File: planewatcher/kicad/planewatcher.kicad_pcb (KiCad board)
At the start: 4 copper layers, 86.1 x 54 mm, 154 parts, among them J1 1PPS_OUT, J2 RF_IN, J3 BMI-S-209-F + C, J4 FPGA BANK 33, J5 FPGA BANK 35 V1.2/V1.3, J6 GPS _IN, U1 LEA-M8T, U10 AD8138, U11 AD9203, U2 AP22653AW6-7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

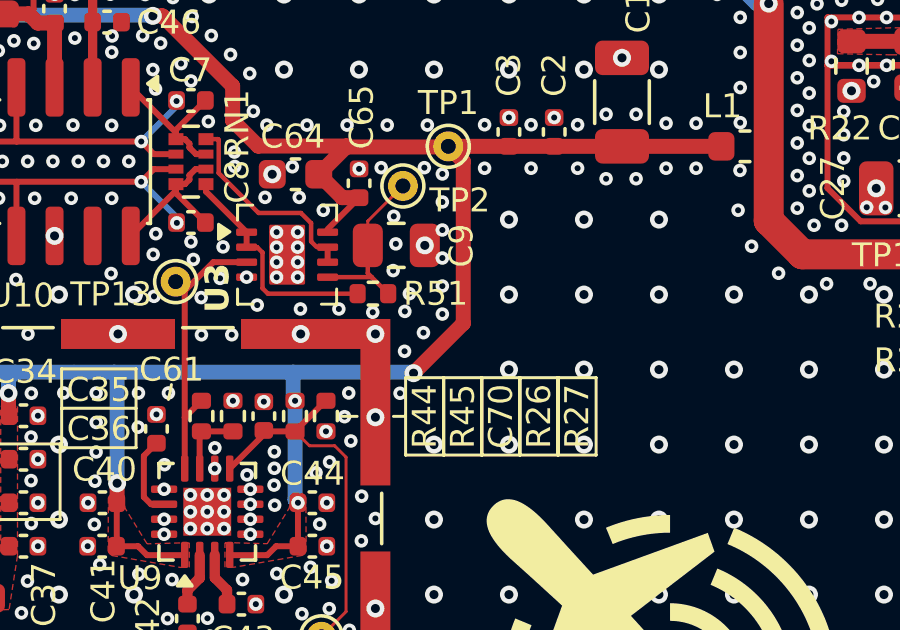
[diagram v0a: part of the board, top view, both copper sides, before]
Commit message: Slow down the LPF to avoid artificially raising the noise-floor baseline in high traffic areas
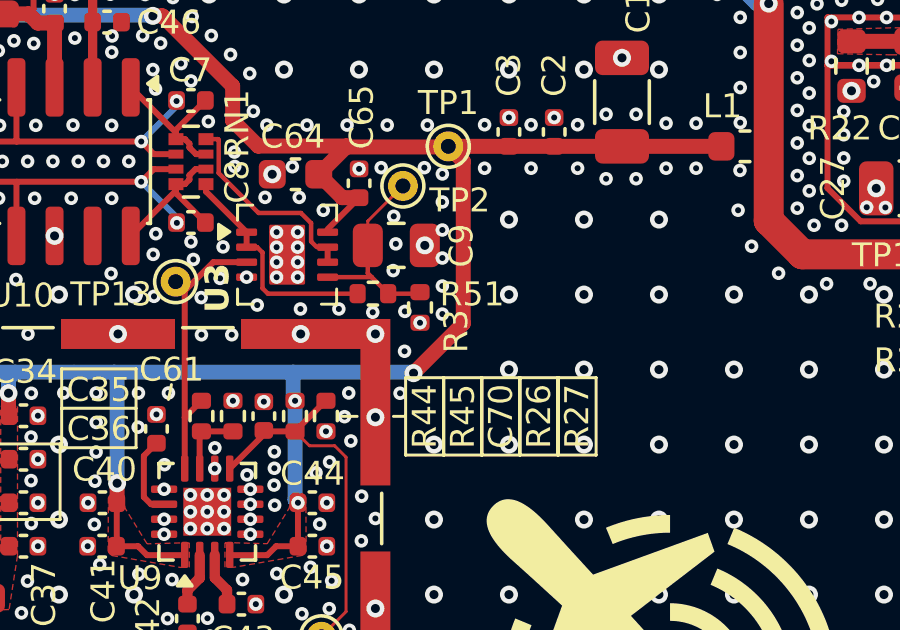
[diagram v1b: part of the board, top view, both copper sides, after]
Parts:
- added R3: R_BASE_GND_DNP, Resistor_SMD:R_0402_1005Metric, F.Cu at (144.5, 90.4)
- C9: value 1µF -> 2.2µF
- R51: value 100kΩ -> 1MΩ
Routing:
- net Net-(U3B-+INB): track 5.83 -> 6.91 mm
- net GND: vias 1851 -> 1850
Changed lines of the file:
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@@
 		)
 	)
+	(footprint "Resistor_SMD:R_0402_1005Metric"
+		(layer "F.Cu")
+		(at 144.535 90.43 -90)
+		(descr "Resistor SMD 0402 (1005 Metric), square (rectangular) end terminal, IPC-7351 nominal, (Body size source: IPC-SM-782 page 72, https://www.pcb-3d.com/wordpress/wp-content/uploads/ipc-sm-782a_amendment_1_and_2.pdf)")
+		(tags "resistor")
+		(property "Reference" "R3"
+			(at 0.79 -1.205 90)
+			(layer "F.SilkS")
+			(effects
+				(font
+					(size 0.8 0.8)
+					(thickness 0.15)
+				)
+			)
+		)
+		(property "Value" "R_BASE_GND_DNP"
+			(at 0 1.17 90)
+			(layer "F.Fab")
+			(effects
+				(font
+					(size 1 1)
+					(thickness 0.15)
+				)
+			)
+		)
+		(property "Datasheet" ""
+			(at 0 0 90)
+			(layer "F.Fab")
+			(hide yes)
+			(effects
+				(font
+					(size 1.27 1.27)
+				)
+			)
+		)
+		(property "Description" "Populating it forces the analog baseline to ground and disables moving-baseline subtraction. Leave DNP for normal operation."
+			(at 0 0 90)
+			(layer "F.Fab")
+			(hide yes)
+			(effects
+				(font
+					(size 1.27 1.27)
+				)
+			)
+		)
+		(property ki_fp_filters "R_*")
+		(sheetname "/ADC_Driver/")
+		(sheetfile "ADC_Driver.kicad_sch")
+		(units
+			(unit
+				(name "A")
+				(pins "1" "2")
+			)
+		)
+		(attr smd exclude_from_pos_files exclude_from_bom dnp)
+		(duplicate_pad_numbers_are_jumpers no)
+		(fp_line
+			(start -0.153641 0.38)
+			(end 0.153641 0.38)
+			(stroke
+				(width 0.12)
+				(type solid)
+			)
+			(layer "F.SilkS")
+		)
+		(fp_line
+			(start -0.153641 -0.38)
+			(end 0.153641 -0.38)
+			(stroke
+				(width 0.12)
+				(type solid)
+			)
+			(layer "F.SilkS")
+		)
+		(fp_rect
+			(start -0.93 -0.47)
+			(end 0.93 0.47)
+			(stroke
+				(width 0.05)
+				(type solid)
+			)
+			(fill no)
+			(layer "F.CrtYd")
+		)
+		(fp_rect
+			(start -0.525 -0.27)
+			(end 0.525 0.27)
+			(stroke
+				(width 0.1)
+				(type solid)
+			)
+			(fill no)
+			(layer "F.Fab")
+		)
+		(fp_text user "${REFERENCE}"
+			(at 0 0 90)
+			(layer "F.Fab")
+			(effects
+				(font
+					(size 0.26 0.26)
+					(thickness 0.04)
+				)
+			)
+		)
+		(pad "1" smd roundrect
+			(at -0.51 0 270)
+			(size 0.54 0.64)
+			(layers "F.Cu" "F.Mask" "F.Paste")
+			(roundrect_rratio 0.25)
+			(net "Net-(U3B-+INB)")
+			(pintype "passive")
+		)
+		(pad "2" smd roundrect
+			(at 0.51 0 270)
+			(size 0.54 0.64)
+			(layers "F.Cu" "F.Mask" "F.Paste")
+			(roundrect_rratio 0.25)
+			(net "GND")
+			(pintype "passive")
+		)
+		(embedded_fonts no)
+		(model "${KICAD10_3DMODEL_DIR}/Resistor_SMD.3dshapes/R_0402_1005Metric.step"
+			(offset
+				(xyz 0 0 0)
+			)
+			(scale
+				(xyz 1 1 1)
+			)
+			(rotate
+				(xyz 0 0 0)
+			)
+		)
+	)
 	(footprint "Capacitor_SMD:C_0402_1005Metric"
 		(layer "F.Cu")
@@
 			)
 		)
-		(property "Value" "1µF"
+		(property "Value" "2.2µF"
 			(at 0 1.68 0)
 			(layer "F.Fab")
@@
 			)
 		)
-		(property "Datasheet" ""
+		(property "Datasheet" "https://www.lcsc.com/datasheet/C5362585.pdf"
 			(at 0 0 0)
 			(layer "F.Fab")
@@
 			)
 		)
-		(property "Description" "CAP CER 1uF 50V X7R 0805"
+		(property "Description" "CAP CER 2.2uF 50V X7R 0805"
 			(at 0 0 0)
 			(layer "F.Fab")
@@
 			)
 		)
-		(property "MPN" "CL21B105KBFNNNE"
+		(property "MPN" "CL21B225KBYVPNE"
 			(at 0 0 0)
 			(unlocked yes)
@@
 			)
 		)
-		(property "lcsc_id" "C28323"
+		(property "lcsc_id" "C5362585"
 			(at 0 0 0)
 			(unlocked yes)
@@
 		(tags "resistor")
 		(property "Reference" "R51"
-			(at -2.09 0 0)
+			(at -3.305 -0.02 0)
 			(layer "F.SilkS")
 			(effects
@@
 			)
 		)
-		(property "Value" "100kΩ"
+		(property "Value" "1MΩ"
 			(at 0 1.17 0)
 			(layer "F.Fab")
@@
 			)
 		)
-		(property "Datasheet" "https://www.lcsc.com/datasheet/C481918.pdf"
+		(property "Datasheet" "https://www.lcsc.com/datasheet/C413126.pdf"
 			(at 0 0 0)
 			(layer "F.Fab")
@@
 			)
 		)
-		(property "Description" "RES 100kΩ ±1% 63mW 0402"
+		(property "Description" "RES 1000000Ω ±1% 0.1W 0402"
 			(at 0 0 0)
 			(layer "F.Fab")
@@
 			)
 		)
-		(property "MPN" "CRCW0402100KFKED"
+		(property "MPN" "ERJ2RKF1004X"
 			(at 0 0 180)
 			(unlocked yes)
@@
 			)
 		)
-		(property "Manufacturer" "VISHAY"
+		(property "Manufacturer" "PANASONIC"
 			(at 0 0 180)
 			(unlocked yes)
@@
 			)
 		)
-		(property "lcsc_id" "C481918"
+		(property "lcsc_id" "C413126"
 			(at 0 0 180)
 			(unlocked yes)
@@
 	)
 	(via
-		(at 144.65 91.27)
+		(at 144.535 90.939998)
 		(size 0.45)
 		(drill 0.2)
@@
 	)
 	(via
-		(at 144.18 89.97)
-		(size 0.45)
-		(drill 0.2)
-		(layers "F.Cu" "B.Cu")
-		(free yes)
-		(net "GND")
-	)
-	(via
 		(at 122.78 80.44)
 		(size 0.45)
@@
 	(segment
 		(start 143.475 89.97)
+		(end 144.485 89.97)
+		(width 0.15)
+		(layer "F.Cu")
+		(net "Net-(U3B-+INB)")
+	)
+	(segment
+		(start 143.475 89.97)
 		(end 142.925 89.42)
 		(width 0.15)
@@
 		(layer "F.Cu")
 		(net "Net-(U3B-+INB)")
+	)
+	(segment
+		(start 144.485 89.97)
+		(end 144.535 89.92)
+		(width 0.15)
+		(layer "F.Cu")
+		(net "Net-(U3B-+INB)")

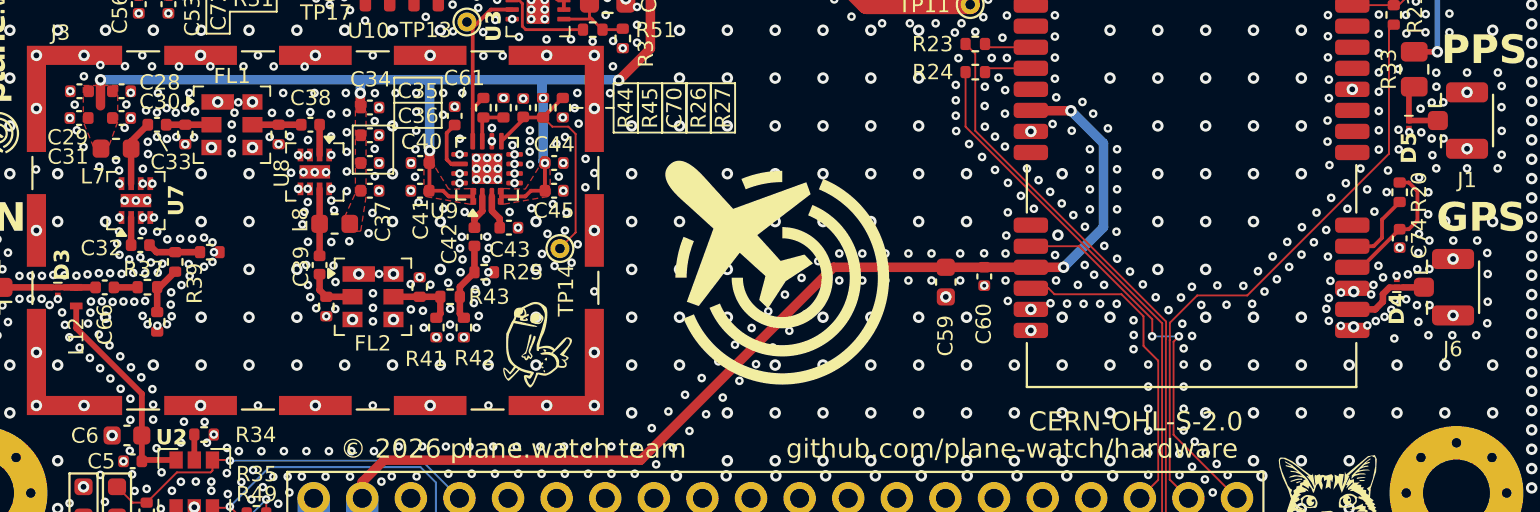
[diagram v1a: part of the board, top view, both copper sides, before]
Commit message: Add RF short to ground on bias-tee supply
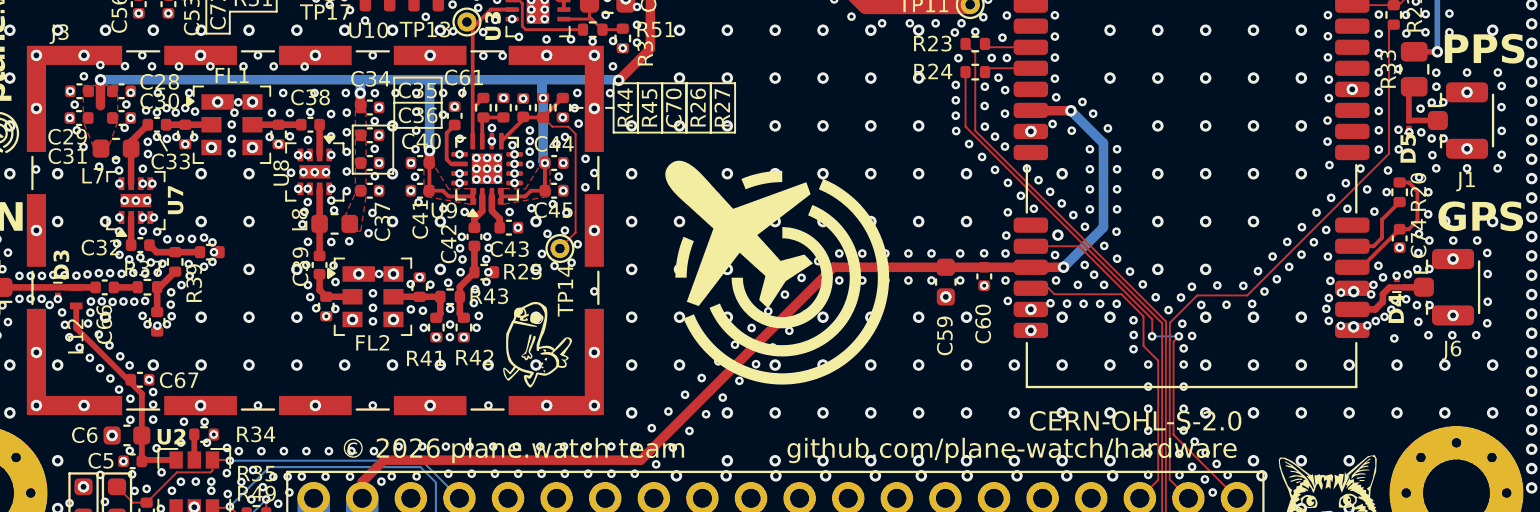
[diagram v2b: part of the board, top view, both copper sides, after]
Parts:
- added C67: 100pF, Capacitor_SMD:C_0402_1005Metric, F.Cu at (119.3, 108.3)
- turned D5 to 90 degrees

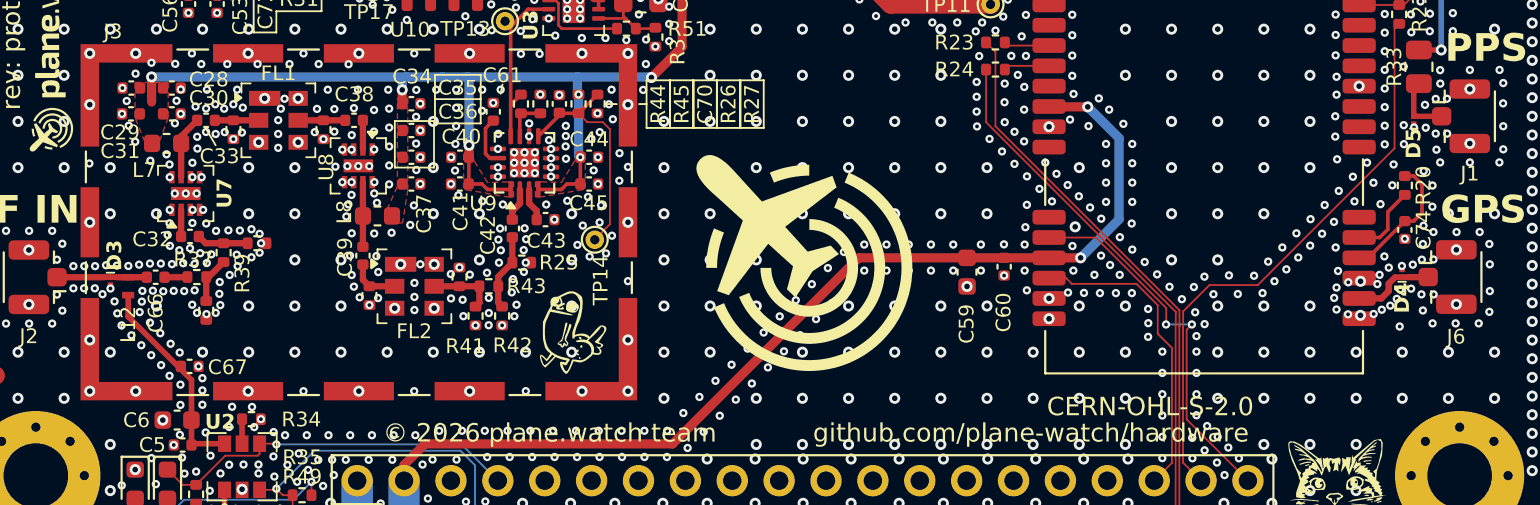
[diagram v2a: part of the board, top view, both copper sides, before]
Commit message: Move C67 closer to L12
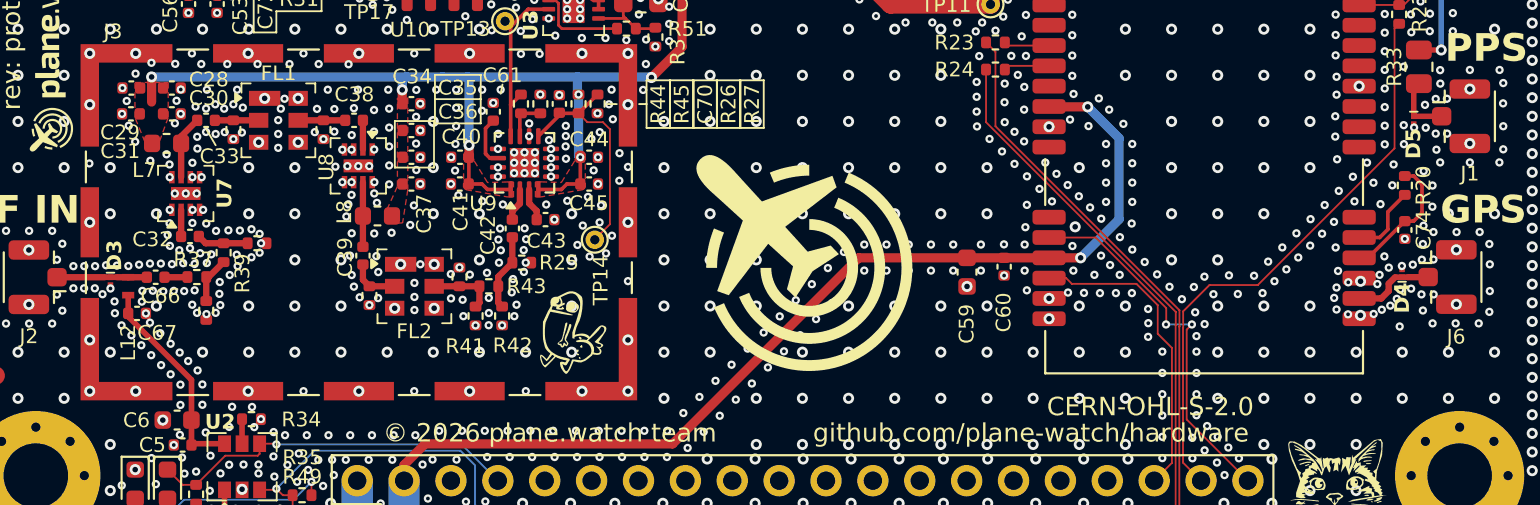
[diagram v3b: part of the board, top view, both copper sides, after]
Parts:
- moved C67 4.04 mm to (116.5, 105.4)
- turned D5 to -90 degrees
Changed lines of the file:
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@@
 		(tags "capacitor")
 		(property "Reference" "C66"
-			(at 0 -1.94 90)
+			(at -0.26 -1.02 180)
 			(layer "F.SilkS")
 			(effects
@@
 		(descr "Footprint for Coilcraft 0402DC, 0402 (1005 Metric) chip inductor")
 		(property "Reference" "L12"
-			(at -2.075 0.0018 90)
+			(at -3.065 0 90)
 			(unlocked yes)
 			(layer "F.SilkS")
@@
 	(footprint "Capacitor_SMD:C_0402_1005Metric"
 		(layer "F.Cu")
-		(at 119.3 108.27)
+		(at 116.45 105.4)
 		(descr "Capacitor SMD 0402 (1005 Metric), square (rectangular) end terminal, IPC-7351 nominal, (Body size source: IPC-SM-782 page 76, https://www.pcb-3d.com/wordpress/wp-content/uploads/ipc-sm-782a_amendment_1_and_2.pdf)")
 		(tags "capacitor")
 		(property "Reference" "C67"
-			(at 2.06 0.05 0)
+			(at 1.09 1.06 0)
 			(layer "F.SilkS")
 			(effects
@@
 	(footprint "planewatcher:ESD8472"
 		(layer "F.Cu")
-		(at 185.6218 94.930001 90)
+		(at 185.6218 94.930001 -90)
 		(descr "X3DFN2, 0.62x0.32x0.24, 0.35P, CASE 152AF, ISSUE C")
 		(property "Reference" "D5"
-			(at -1.259999 -0.0118 90)
+			(at 1.269999 0.0218 90)
 			(unlocked yes)
 			(layer "F.SilkS")
@@
 		)
 		(property "Value" "ESD8472MUT5G"
-			(at 0 0.99 90)
+			(at 0 0.99 270)
 			(unlocked yes)
 			(layer "F.Fab")
@@
 		)
 		(property "Datasheet" "https://www.onsemi.com/download/data-sheet/pdf/esd8472-d.pdf"
-			(at 0 0 90)
+			(at 0 0 270)
 			(unlocked yes)
 			(layer "F.Fab")
@@
 		)
 		(property "Description" "14V Clamp 3A (8/20µs) Ipp Tvs Diode Surface Mount 2-X3DFN (0.6x0.3) (0201)"
-			(at 0 0 90)
+			(at 0 0 270)
 			(unlocked yes)
 			(layer "F.Fab")
@@
 		)
 		(property "Package" "2-X3DFN (0.6x0.3) (0201)"
-			(at 0 0 90)
+			(at 0 0 270)
 			(unlocked yes)
 			(layer "F.Fab")
@@
 		)
 		(property "MPN" "ESD8472MUT5G"
-			(at 0 0 90)
+			(at 0 0 270)
 			(unlocked yes)
 			(layer "F.Fab")
@@
 		)
 		(property "Manufacturer" "onsemi"
-			(at 0 0 90)
+			(at 0 0 270)
 			(unlocked yes)
 			(layer "F.Fab")
@@
 		)
 		(property "Purpose" "Low-capacitance ESD/TVS protection for the external 1PPS connector. Clamps ESD/transient events from the coax centre pin to ground. Place close to the connector."
-			(at 0 0 90)
+			(at 0 0 270)
 			(unlocked yes)
 			(layer "F.Fab")
@@
 		)
 		(property "Notes" ""
-			(at 0 0 90)
+			(at 0 0 270)
 			(unlocked yes)
 			(layer "F.Fab")
@@
 		)
 		(property "lcsc_id" "C133346"
-			(at 0 0 90)
+			(at 0 0 270)
 			(unlocked yes)
 			(layer "F.Fab")
@@
 		)
 		(property "Sim.Device" ""
-			(at 0 0 90)
+			(at 0 0 270)
 			(unlocked yes)
 			(layer "F.Fab")
@@
 		)
 		(property "Sim.Type" ""
-			(at 0 0 90)
+			(at 0 0 270)
 			(unlocked yes)
 			(layer "F.Fab")
@@
 		)
 		(fp_text user "${REFERENCE}"
-			(at 0 2.49 90)
+			(at 0 2.49 270)
 			(unlocked yes)
 			(layer "F.Fab")
@@
 		)
 		(pad "1" smd rect
-			(at -0.215 0 90)
+			(at -0.215 0 270)
 			(size 0.31 0.3)
 			(layers "F.Cu" "F.Mask" "F.Paste")
@@
 		)
 		(pad "2" smd rect
-			(at 0.215 0 90)
+			(at 0.215 0 270)
 			(size 0.31 0.3)
 			(layers "F.Cu" "F.Mask" "F.Paste")
@@
 	)
 	(via
-		(at 115.38 105.4)
+		(at 115.25 105.39)
 		(size 0.45)
 		(drill 0.2)
@@
 	)
 	(via
-		(at 119.780002 108.27)
+		(at 119.73 108.49)
 		(size 0.45)
 		(drill 0.2)
@@
 	)
 	(via
-		(at 119.99 109.57)
-		(size 0.45)
-		(drill 0.2)
-		(layers "F.Cu" "B.Cu")
-		(free yes)
-		(net "GND")
-	)
-	(via
 		(at 160 95)
 		(size 0.6)
@@
 	)
 	(via
-		(at 119.99 108.91)
+		(at 119.99 109.25)
 		(size 0.45)
 		(drill 0.2)
@@
 	)
 	(via
-		(at 118.21 108.78)
+		(at 118.27 108.7)
 		(size 0.45)
 		(drill 0.2)
@@
 	)
 	(via
-		(at 116.59 105.33)
+		(at 116.930002 105.4)
 		(size 0.45)
 		(drill 0.2)
@@
 		(size 0.45)
 		(drill 0.2)
+		(layers "F.Cu" "B.Cu")
+		(free yes)
+		(net "GND")
+	)
+	(via
+		(at 119.22 107.98)
+		(size 0.45)
+		(drill 0.2)
